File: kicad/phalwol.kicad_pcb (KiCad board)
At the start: 2 copper layers, 169.6 x 117.1 mm, 114 parts, among them J1 AudioJack4, SW1 SW_Push, SW10 SW_Push, SW11 SW_Push, SW12 SW_Push, SW13 SW_Push, SW14 SW_Push, SW15 SW_Push, SW16 SW_Push, SW17 SW_Push, SW18 SW_Push, SW19 SW_Push, SW2 SW_Push, SW20 SW_Push, SW21 SW_Push, SW22 SW_Push, SW23 SW_Push, SW24 SW_Push, SW25 SW_Push, SW26 SW_Push, SW27 SW_Push, SW28 SW_Push, SW29 SW_Push, SW3 SW_Push, SW30 SW_Push, SW31 SW_Push, SW32 SW_Push, SW33 SW_Push, SW34 SW_Push, SW35 SW_Push, SW36 SW_Push, SW37 SW_Push, SW38 SW_Push, SW39 SW_Push, SW4 SW_Push, SW40 SW_Push, SW41 SW_Push, SW5 SW_Push, SW6 SW_Push, SW7 SW_Push, SW8 SW_Push, SW9 SW_Push, U1 ProMicro

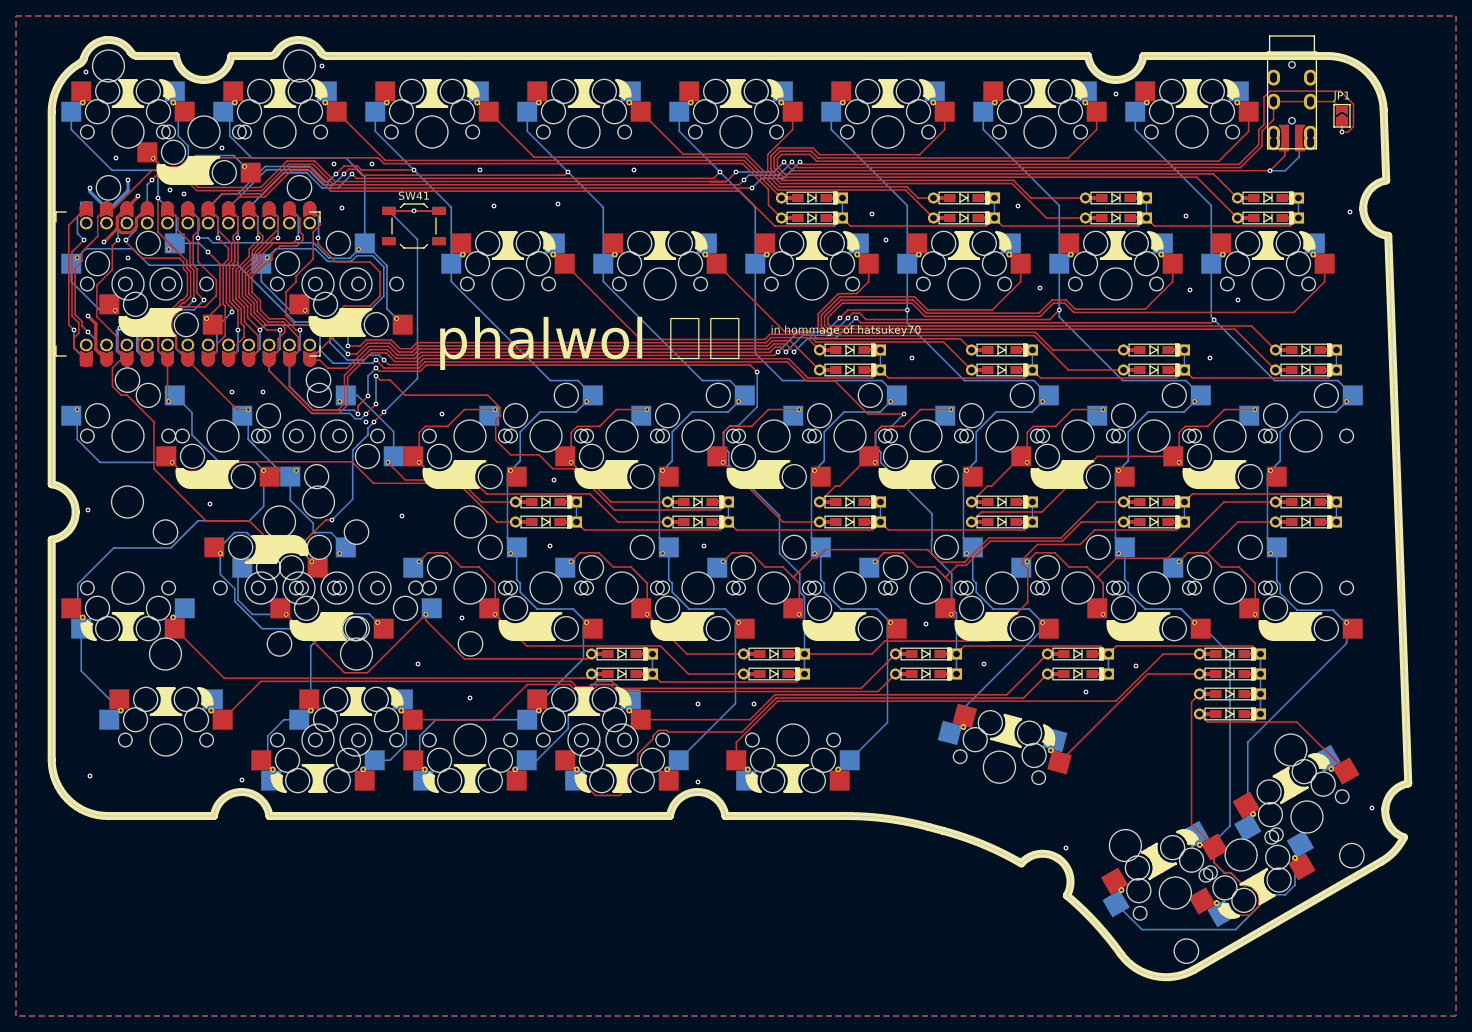
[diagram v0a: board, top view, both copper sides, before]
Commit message: change modifier cluster to fixed one
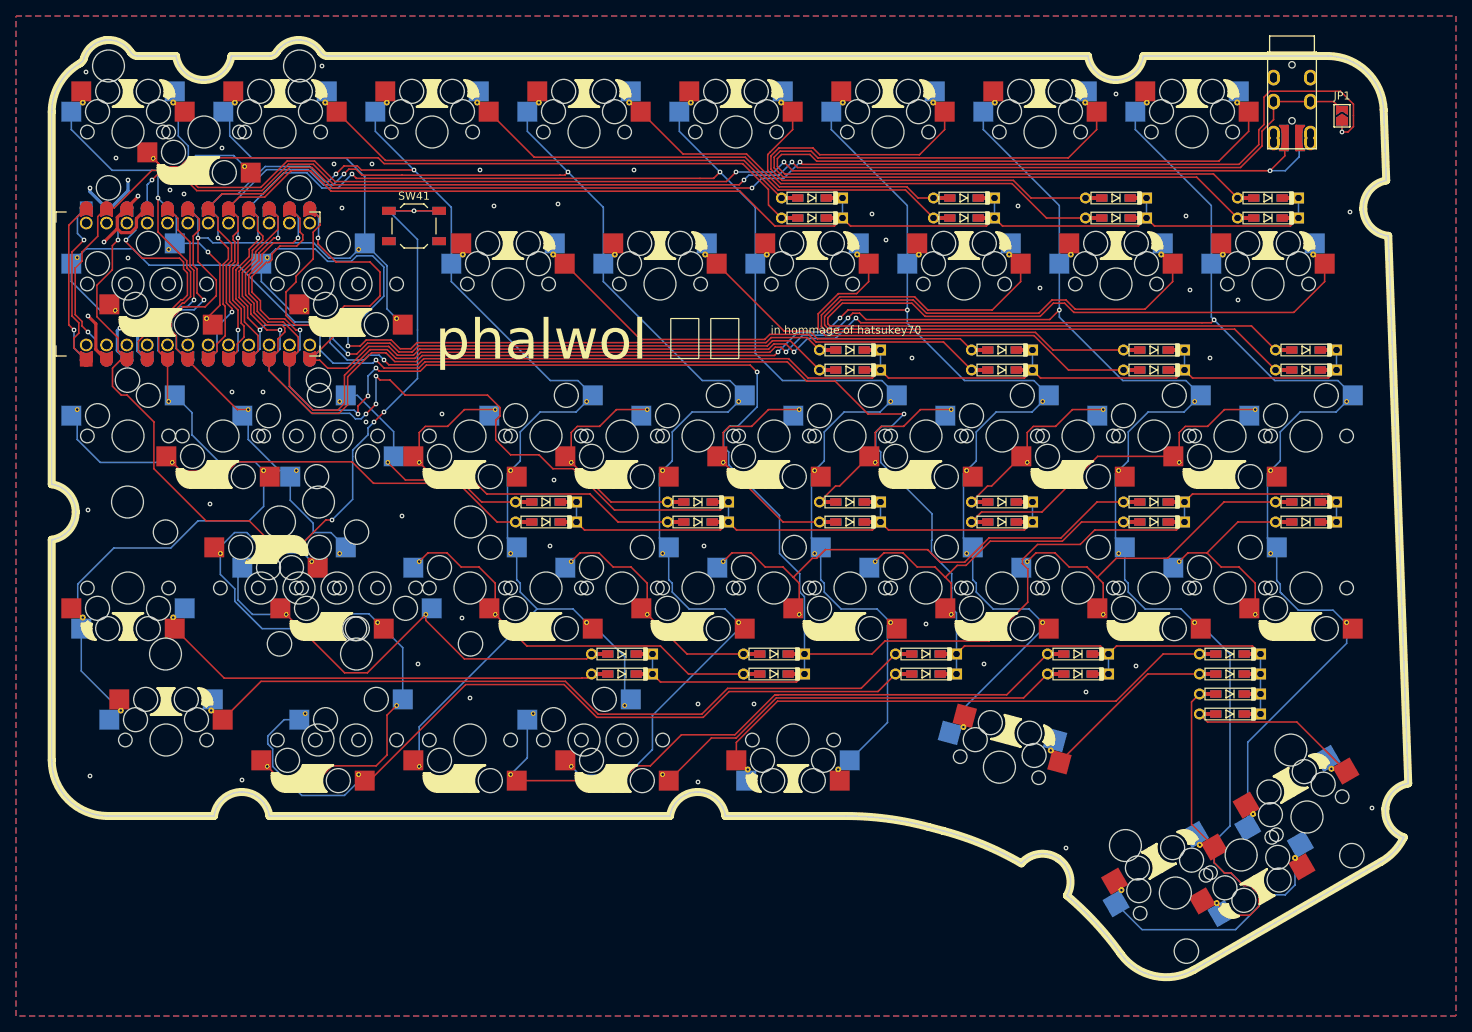
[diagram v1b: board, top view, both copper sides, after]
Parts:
- SW34, SW35, SW36: footprint yubuGadgetsFootpints:MX_Hotswap_FootprintPropertyFix_Guided -> yubuGadgetsFootpints:MX_HotswapOneside_Via_Guided
- SW34, SW35: footprint yubuGadgetsFootpints:MX_Hotswap_FootprintPropertyFix_Guided -> yubuGadgetsFootpints:MX_HotswapOneside_Via_Guided; moved to B.Cu
- turned SW34 to 180 degrees
- turned SW35 to 180 degrees
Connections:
- SW36 pad 1: COL4 -> Net-(D36-A)
- SW36 pad 2: Net-(D36-A) -> COL4
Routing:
- net Net-(D34-A): track 73.2 -> 97.9 mm
- net Net-(D36-A): track 69.1 -> 52.9 mm
- net COL2: track 187.8 -> 200.3 mm
- net COL4: track 177.8 -> 189.8 mm
- net Net-(D35-A): track 73.5 -> 81.0 mm
- net COL3: track 173.1 -> 179.3 mm
- net Net-(D33-A): track 88.8 -> 90.9 mm
- net SERIAL: track 188.1 -> 186.0 mm
